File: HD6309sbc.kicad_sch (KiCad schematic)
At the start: 18 parts, among them J1 Conn_01x02_Male, J3 Conn_01x02_Male, U1 HD63C09, U11 74HC02, U12 74HC21, U13 74HC21, U4 UM61256FK, U6 27C256, U7 74HC04, U8 74HC00

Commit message: modify address logic for mapped registers
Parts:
- removed U12: 74HC21, Package_SO:SO-14_3.9x8.65mm_P1.27mm, symbol 74xx:74LS21
- added unit 4 of U11
- added U12: 74AHC1G08, Package_SO:TSOP-5_1.65x3.05mm_P0.95mm, symbol 74xGxx:74AHC1G08
- added U14, U15: 74HC21D, Package_SO:SOIC-14_3.9x8.7mm_P1.27mm, symbol 74xx:74LS21
- C3: value 1uF -> 100uF; DigiKey (none) -> 490-GRM21BR60J107ME15KCT-ND
- R2: value R -> 2.2K; DigiKey (none) -> 2019-RK73H2ATTD2201FCT-ND
- U13: value 74HC21 -> 74HC21D; footprint Package_SO:SO-14_3.9x8.65mm_P1.27mm -> Package_SO:SOIC-14_3.9x8.7mm_P1.27mm; DigiKey (none) -> 296-8265-5-ND
- U7: value 74HC04 -> 74HC04D; footprint Package_SO:SO-14_3.9x8.65mm_P1.27mm -> Package_SO:SOIC-14_3.9x8.7mm_P1.27mm; DigiKey (none) -> 74HC04DCT-ND
- U8: value 74HC00 -> 74HC00D; footprint Package_SO:SO-14_3.9x8.65mm_P1.27mm -> Package_SO:SOIC-14_3.9x8.7mm_P1.27mm; DigiKey (none) -> 74HC00DCT-ND
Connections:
- net +5V: now also U12.5 (VCC), U14.14 (VCC), U15.14 (VCC)
- net A15: now also U12.2; no longer U8.4
- net GND: now also U12.3 (GND), U14.7 (GND), U15.7 (GND)
- net at U8.11: now also U12.1
- net MAPPED_MEM: now reaches U8.12
- net MAPPED_MEM: now also U8.13
- new net: U12.4, U8.4
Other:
- moved on the sheet: C5, U6, U8B, U8D

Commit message: fixes
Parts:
- added R3, R4, R5, R6: 4.7k, Resistor_SMD:R_0805_2012Metric_Pad1.20x1.40mm_HandSolder, symbol Device:R
- RN1, RN2, RN3: value R_Network08 -> 4K7
- U6: value 27C256 -> 28C256
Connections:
- net +5V: now also U6.1 (VPP), R3.1, R4.1, R5.1, R6.1
- net ~{FIRQ}: now also R5.2
- net ~{HALT}: now also R3.2
- net ~{IRQ}: now also R4.2
- net ~{NMI}: now also R6.2
- no-connect marks 9 -> 8
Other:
- moved on the sheet: RN1, RN2, RN3

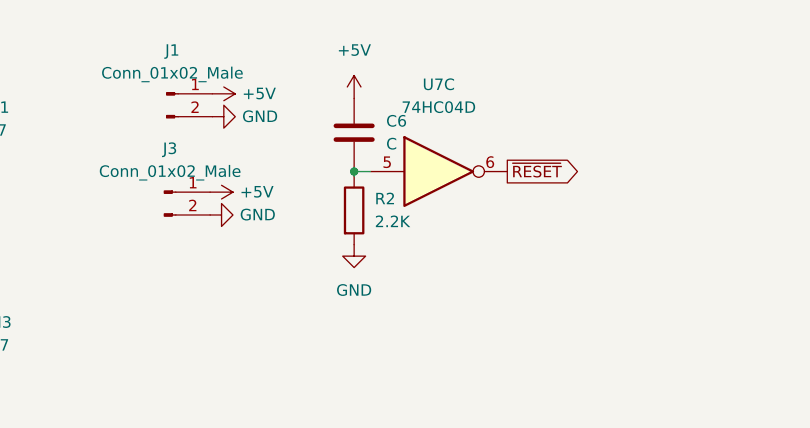
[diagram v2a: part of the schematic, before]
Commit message: set reset cap value
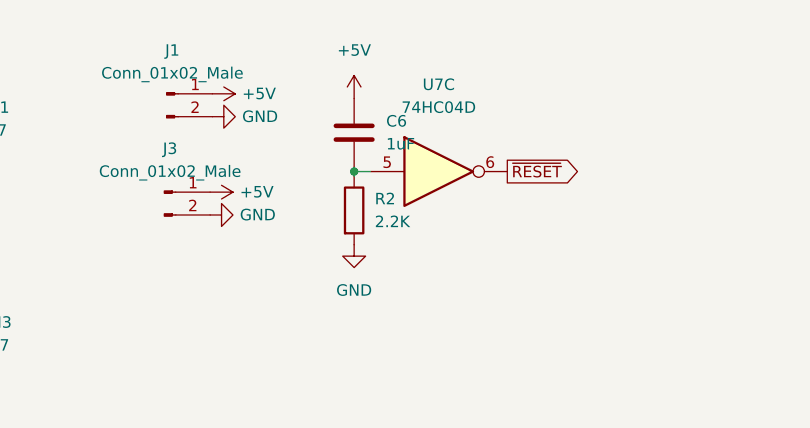
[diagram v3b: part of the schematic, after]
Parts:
- C6: value C -> 1uF
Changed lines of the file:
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@@
       (effects (font (size 1.27 1.27)) (justify left))
     )
-    (property "Value" "C" (id 1) (at 158.242 26.9239 0)
+    (property "Value" "1uF" (id 1) (at 158.242 26.9239 0)
       (effects (font (size 1.27 1.27)) (justify left))
     )
@@
     )
     (path "/e30abfee-1dd8-4d26-93f4-39c0300bc9cf"
-      (reference "C6") (unit 1) (value "C") (footprint "Capacitor_SMD:C_0805_2012Metric")
+      (reference "C6") (unit 1) (value "1uF") (footprint "Capacitor_SMD:C_0805_2012Metric")
     )
     (path "/7fb0b11a-d520-4ab4-8aaa-1ba47fc9417e/509a6177-dcb1-4aa2-8fa1-ddb7dda29eae"

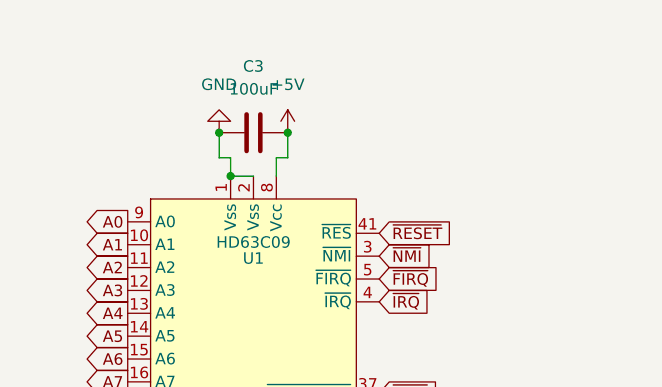
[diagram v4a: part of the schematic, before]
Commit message: use handsolder pads
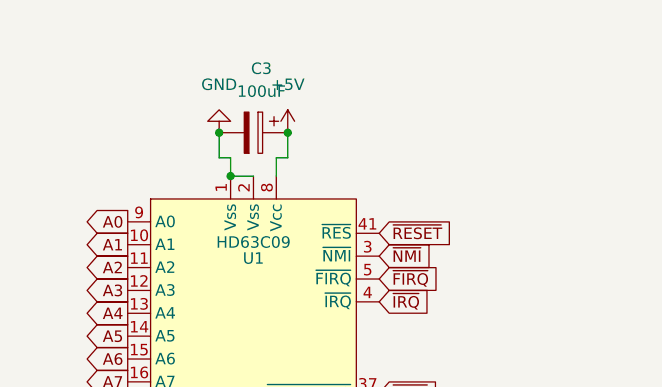
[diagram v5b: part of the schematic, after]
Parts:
- removed C3: 100uF, Capacitor_SMD:C_0805_2012Metric, symbol Device:C
- added C3: 100uF, Capacitor_SMD:CP_Elec_6.3x5.8, symbol Device:C_Polarized
- C2, C5, C6: footprint Capacitor_SMD:C_0805_2012Metric -> Capacitor_SMD:C_0805_2012Metric_Pad1.18x1.45mm_HandSolder
- R2: footprint Resistor_SMD:R_0805_2012Metric -> Resistor_SMD:R_0805_2012Metric_Pad1.20x1.40mm_HandSolder
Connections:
- net +5V: now also C3.1
- net GND: now also C3.2
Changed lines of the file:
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@@
 (kicad_sch (version 20211123) (generator eeschema)
   (paper "A4")
+  (junction (at 35.306 25.654) (diameter 0) (color 0 0 0 0)
+  )
   (junction (at 147.574 132.08) (diameter 0) (color 0 0 0 0)
   )
+  (junction (at 42.926 25.654) (diameter 0) (color 0 0 0 0)
+  )
   (junction (at 36.576 30.48) (diameter 0) (color 0 0 0 0)
   )
   (junction (at 38.1 191.262) (diameter 0) (color 0 0 0 0)
   )
-  (junction (at 42.926 25.654) (diameter 0) (color 0 0 0 0)
-  )
   (junction (at 147.574 187.96) (diameter 0) (color 0 0 0 0)
-  )
-  (junction (at 35.306 25.654) (diameter 0) (color 0 0 0 0)
   )
   (junction (at 154.686 29.972) (diameter 0) (color 0 0 0 0)
@@
       (effects (font (size 1.27 1.27)) (justify left))
     )
-    (property "Footprint" "Capacitor_SMD:C_0805_2012Metric" (id 2) (at 16.2052 174.498 0)
+    (property "Footprint" "Capacitor_SMD:C_0805_2012Metric_Pad1.18x1.45mm_HandSolder" (id 2) (at 16.2052 174.498 0)
       (effects (font (size 1.27 1.27)) hide)
     )
@@
     (pin "7")
   )
+  (symbol (lib_id "Device:C_Polarized") (at 39.116 25.654 270) (unit 1)
+    (in_bom yes) (on_board yes) (fields_autoplaced)
+    (property "Reference" "C3" (id 0) (at 40.005 18.542 90))
+    (property "Value" "100uF" (id 1) (at 40.005 21.082 90))
+    (property "Footprint" "Capacitor_SMD:CP_Elec_6.3x5.8" (id 2) (at 35.306 26.6192 0)
+      (effects (font (size 1.27 1.27)) hide)
+    )
+    (property "Datasheet" "~" (id 3) (at 39.116 25.654 0)
+      (effects (font (size 1.27 1.27)) hide)
+    )
+    (pin "1")
+    (pin "2")
+  )
   (symbol (lib_id "power:GND") (at 154.686 38.1 0) (unit 1)
     (in_bom yes) (on_board yes) (fields_autoplaced)
@@
       (effects (font (size 1.27 1.27)) (justify left))
     )
-    (property "Footprint" "Capacitor_SMD:C_0805_2012Metric" (id 2) (at 169.1132 161.544 0)
+    (property "Footprint" "Capacitor_SMD:C_0805_2012Metric_Pad1.18x1.45mm_HandSolder" (id 2) (at 169.1132 161.544 0)
       (effects (font (size 1.27 1.27)) hide)
     )
@@
     )
     (pin "1")
-  )
-  (symbol (lib_id "Device:C") (at 39.116 25.654 270) (unit 1)
-    (in_bom yes) (on_board yes) (fields_autoplaced)
-    (property "Reference" "C3" (id 0) (at 39.116 18.288 90))
-    (property "Value" "100uF" (id 1) (at 39.116 20.828 90))
-    (property "Footprint" "Capacitor_SMD:C_0805_2012Metric" (id 2) (at 35.306 26.6192 0)
-      (effects (font (size 1.27 1.27)) hide)
-    )
-    (property "Datasheet" "https://search.murata.co.jp/Ceramy/image/img/A01X/G101/ENG/GRM21BR60J107ME15-01A.pdf" (id 3) (at 39.116 25.654 0)
-      (effects (font (size 1.27 1.27)) hide)
-    )
-    (property "DigiKey" "490-GRM21BR60J107ME15KCT-ND" (id 4) (at 39.116 25.654 90)
-      (effects (font (size 1.27 1.27)) hide)
-    )
-    (pin "1")
-    (pin "2")
   )
   (symbol (lib_id "power:+5V") (at 280.162 139.954 0) (unit 1)
@@
       (effects (font (size 1.27 1.27)) (justify left))
     )
-    (property "Footprint" "Capacitor_SMD:C_0805_2012Metric" (id 2) (at 155.6512 29.464 0)
+    (property "Footprint" "Capacitor_SMD:C_0805_2012Metric_Pad1.18x1.45mm_HandSolder" (id 2) (at 155.6512 29.464 0)
       (effects (font (size 1.27 1.27)) hide)
     )
@@
       (effects (font (size 1.27 1.27)) (justify left))
     )
-    (property "Footprint" "Resistor_SMD:R_0805_2012Metric" (id 2) (at 152.908 34.29 90)
+    (property "Footprint" "Resistor_SMD:R_0805_2012Metric_Pad1.20x1.40mm_HandSolder" (id 2) (at 152.908 34.29 90)
       (effects (font (size 1.27 1.27)) hide)
     )
@@
     )
     (path "/03b0e509-a9b7-42e3-b8aa-5c27956ccf70"
-      (reference "C2") (unit 1) (value "1uF") (footprint "Capacitor_SMD:C_0805_2012Metric")
-    )
-    (path "/3dc21636-5faf-4778-8c29-676dd404313f"
-      (reference "C3") (unit 1) (value "100uF") (footprint "Capacitor_SMD:C_0805_2012Metric")
+      (reference "C2") (unit 1) (value "1uF") (footprint "Capacitor_SMD:C_0805_2012Metric_Pad1.18x1.45mm_HandSolder")
+    )
+    (path "/17e7e0e7-c5a5-48c2-a54d-a32ad4ff74e7"
+      (reference "C3") (unit 1) (value "100uF") (footprint "Capacitor_SMD:CP_Elec_6.3x5.8")
     )
     (path "/2d23715c-870a-4052-bbc4-d4a0af944087"
-      (reference "C5") (unit 1) (value "1uF") (footprint "Capacitor_SMD:C_0805_2012Metric")
+      (reference "C5") (unit 1) (value "1uF") (footprint "Capacitor_SMD:C_0805_2012Metric_Pad1.18x1.45mm_HandSolder")
     )
     (path "/e30abfee-1dd8-4d26-93f4-39c0300bc9cf"
-      (reference "C6") (unit 1) (value "1uF") (footprint "Capacitor_SMD:C_0805_2012Metric")
+      (reference "C6") (unit 1) (value "1uF") (footprint "Capacitor_SMD:C_0805_2012Metric_Pad1.18x1.45mm_HandSolder")
     )
     (path "/7fb0b11a-d520-4ab4-8aaa-1ba47fc9417e/509a6177-dcb1-4aa2-8fa1-ddb7dda29eae"
@@
     )
     (path "/7fb0b11a-d520-4ab4-8aaa-1ba47fc9417e/8a569ddf-9b87-435b-bf88-01c902274bca"
-      (reference "R1") (unit 1) (value "2.2k") (footprint "Resistor_SMD:R_0805_2012Metric")
+      (reference "R1") (unit 1) (value "2.2k") (footprint "Resistor_SMD:R_0805_2012Metric_Pad1.20x1.40mm_HandSolder")
     )
     (path "/e6574e3b-4bfb-481f-a81a-d4d7d62df2dd"
-      (reference "R2") (unit 1) (value "2.2K") (footprint "Resistor_SMD:R_0805_2012Metric")
+      (reference "R2") (unit 1) (value "2.2K") (footprint "Resistor_SMD:R_0805_2012Metric_Pad1.20x1.40mm_HandSolder")
     )
     (path "/3598dd16-7772-4af6-9a8b-206ac6a85376"

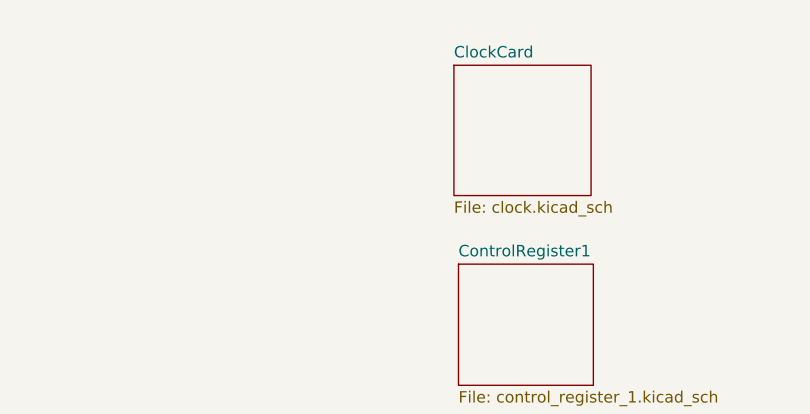
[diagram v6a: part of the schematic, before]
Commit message: add diagnostics port
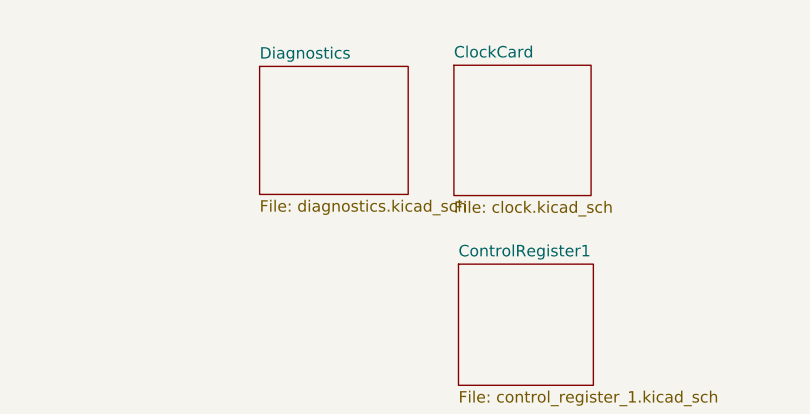
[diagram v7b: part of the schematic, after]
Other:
- added sheet Diagnostics (diagnostics.kicad_sch)
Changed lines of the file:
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@@
+    )
+  )
+  (sheet (at 226.822 18.288) (size 16.51 14.224) (fields_autoplaced)
+    (stroke (width 0.1524) (type solid))
+    (fill (color 0 0 0 0.0000))
+    (property "Sheetname" "Diagnostics" (at 226.822 17.5764 0)
+      (effects (font (size 1.27 1.27)) (justify left bottom))
+    )
+    (property "Sheetfile" "diagnostics.kicad_sch" (at 226.822 33.0966 0)
+      (effects (font (size 1.27 1.27)) (justify left top))
+    )
+    (instances
+      (project "HD6309sbc"
+        (path "/b6976bcd-dc73-4942-aa19-f7adbf9104c7" (page "5"))
+      )
     )
   )

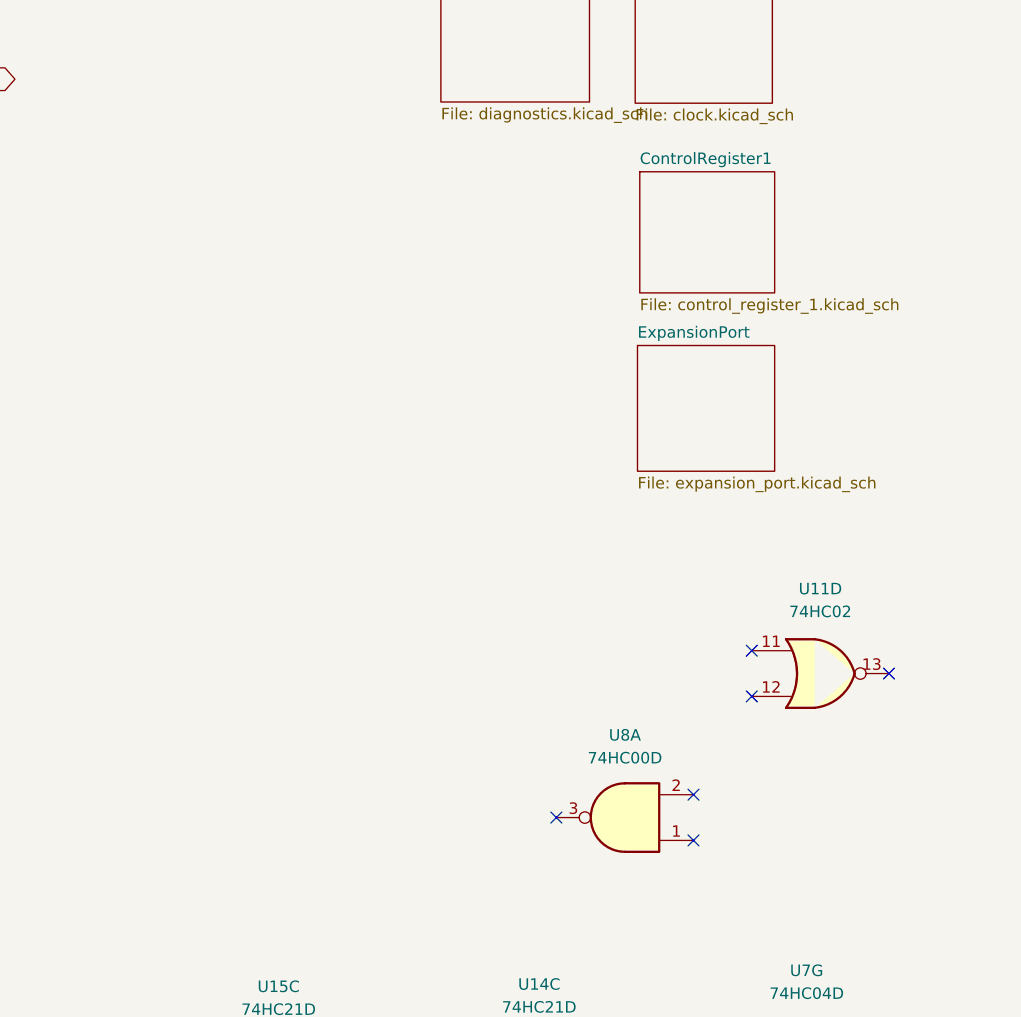
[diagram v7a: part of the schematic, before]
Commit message: tidy up component placing
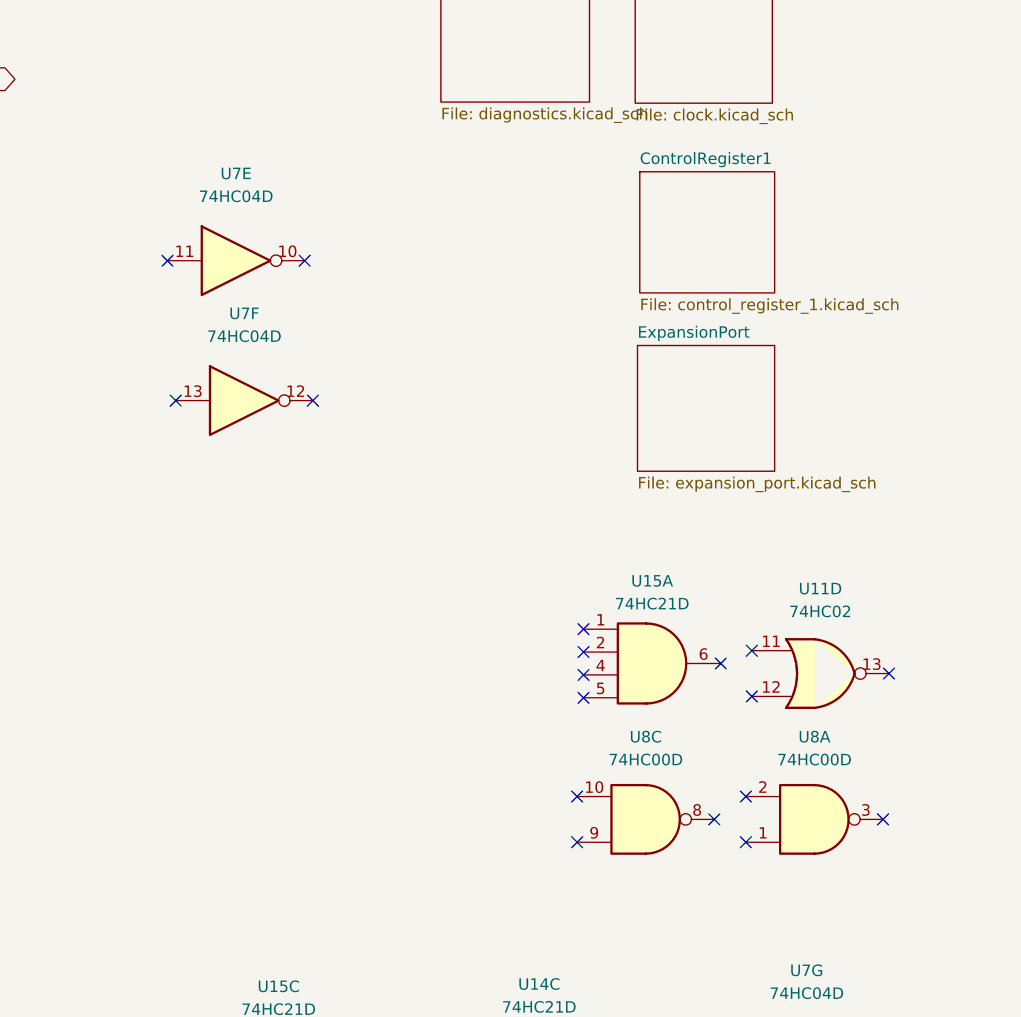
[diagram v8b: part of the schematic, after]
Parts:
- added unit 1 of U15
- added unit 6 of U7
- added unit 5 of U7
- added unit 3 of U8
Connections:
- no-connect marks 8 -> 20
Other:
- moved on the sheet: U8A
